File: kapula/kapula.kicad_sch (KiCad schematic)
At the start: 157 parts, among them J1 Conn_02x10_Odd_Even, J12 U.FL, J13 U.FL, J3 U.FL, J5 U.FL, J9 U.FL, Q1 AO3401A, Q1 BSS84, Q2 AO3401A, Q3 AO3400A, Q5 AO3400A, Q6 AO3400A, T1 BW21S7511A01TF, T2 BW21S7511A01TF, T3 BW21S7511A01TF, T4 BW21S7511A01TF, U1 XC6206P332MR, U2 TP4054, U3 DW01+G, U5 EFR32FG14P233F256GM48-B, U6 XA213-G4J, X1 DSB221SDN, Y1 32768 Hz

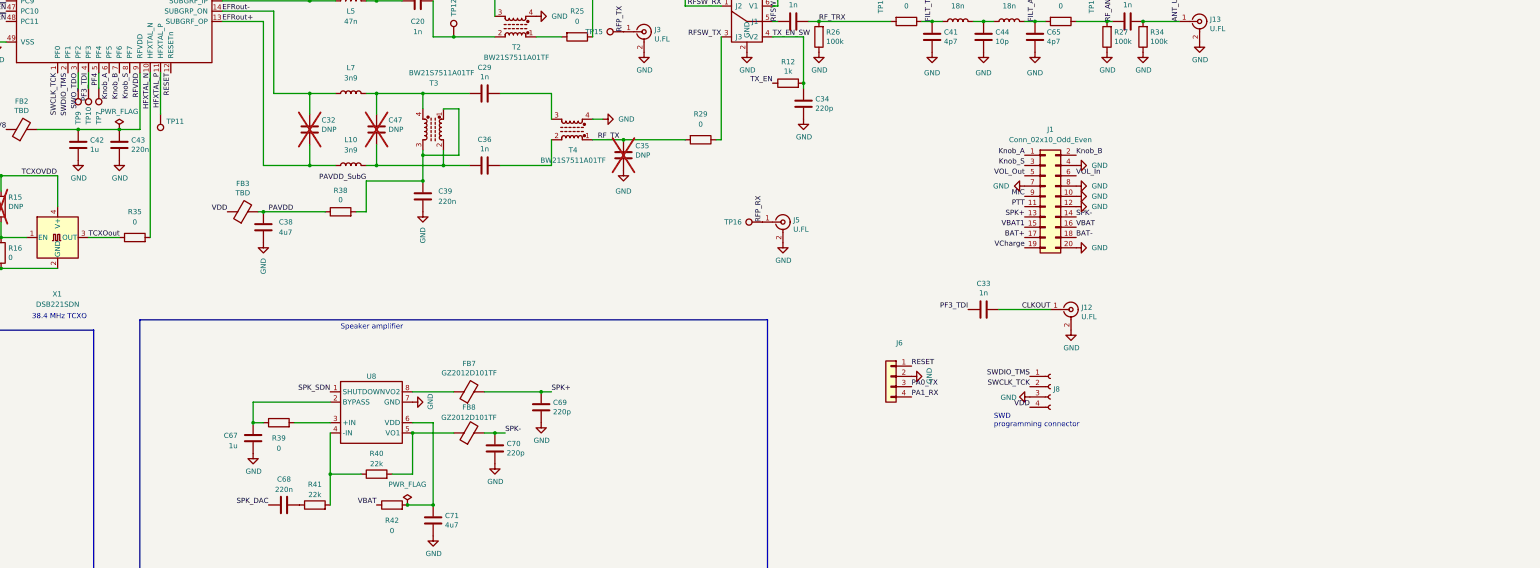
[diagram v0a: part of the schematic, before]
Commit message: Move components to make more space
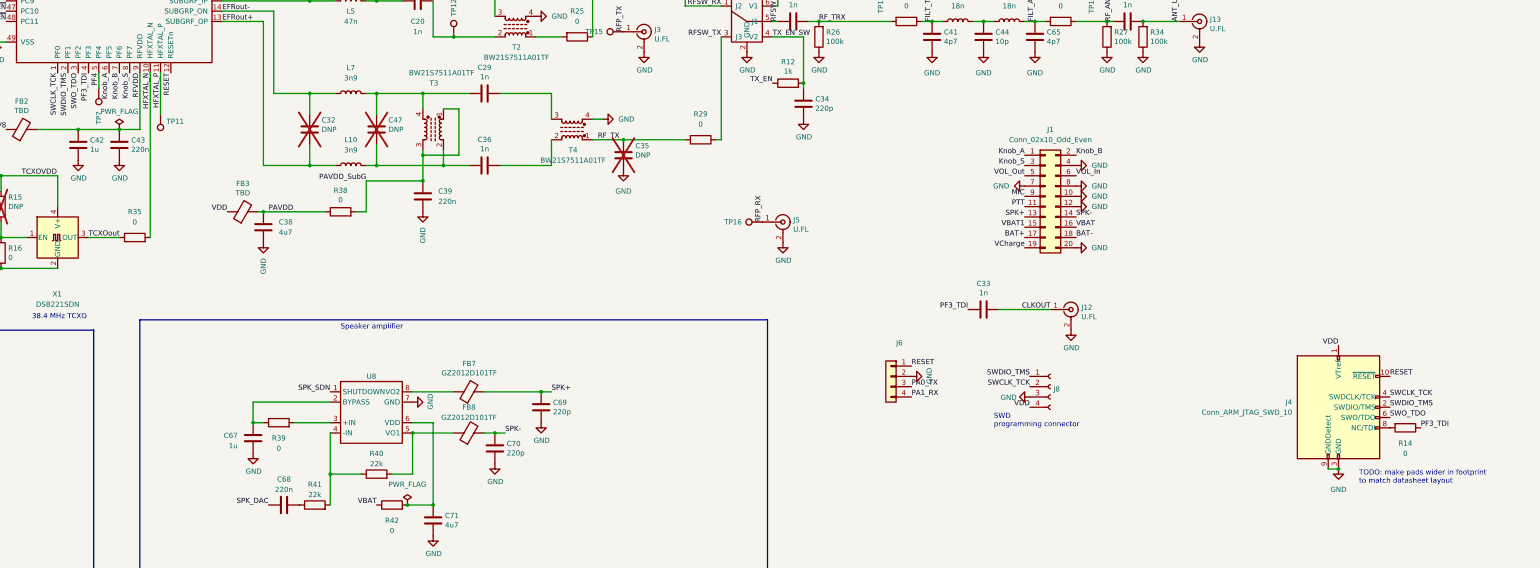
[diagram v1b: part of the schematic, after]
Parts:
- removed TP10, TP9: ~, TestPoint:TestPoint_Pad_D1.0mm, symbol Connector:TestPoint
- added J4: Conn_ARM_JTAG_SWD_10, Connector_PinHeader_1.27mm:PinHeader_2x05_P1.27mm_Vertical_SMD, symbol Connector:Conn_ARM_JTAG_SWD_10
- added R14: 0, kapula:R_0402_to_0603_HandSolder, symbol Device:R
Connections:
- net GND: now also J4.3 (GND), J4.5 (GND), J4.9 (GNDDetect)
- net PF3_TDI: now also R14.1
- net RESET: now also J4.10 (~{RESET})
- net SWCLK_TCK: now also J4.4 (SWDCLK/TCK)
- net SWDIO_TMS: now also J4.2 (SWDIO/TMS)
- net SWO_TDO: now also J4.6 (SWO/TDO)
- net VDD: now also J4.1 (VTref)
- new net: J4.8 (NC/TDI), R14.2
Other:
- note added: "TODO: make pads wider in footprint to match datasheet layout"
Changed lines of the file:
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@@
   (junction (at 201.93 127) (diameter 0) (color 0 0 0 0)
   )
+  (junction (at 439.42 252.73) (diameter 0) (color 0 0 0 0)
+  )
   (junction (at 173.99 82.55) (diameter 0) (color 0 0 0 0)
   )
@@
     (stroke (width 0) (type default))
   )
-  (wire (pts (xy 128.27 154.94) (xy 128.27 158.75))
-    (stroke (width 0) (type default))
-  )
   (wire (pts (xy 340.36 49.53) (xy 340.36 48.26))
     (stroke (width 0) (type default))
@@
     (stroke (width 0) (type default))
   )
+  (wire (pts (xy 436.88 252.73) (xy 439.42 252.73))
+    (stroke (width 0) (type default))
+  )
   (wire (pts (xy 353.06 30.48) (xy 365.76 30.48))
     (stroke (width 0) (type default))
@@
     (stroke (width 0) (type default))
   )
-  (wire (pts (xy 130.81 158.75) (xy 130.81 154.94))
-    (stroke (width 0) (type default))
-  )
   (wire (pts (xy 176.53 85.09) (xy 229.87 85.09))
     (stroke (width 0) (type default))
@@
     (effects (font (size 1.27 1.27)) (justify left bottom))
   )
+  (text "TODO: make pads wider in footprint\nto match datasheet layout"
+    (at 444.5 256.54 0)
+    (effects (font (size 1.27 1.27)) (justify left bottom))
+  )
   (text "38.4 MHz TCXO" (at 116.84 215.9 0)
     (effects (font (size 1.27 1.27)) (justify left bottom))
@@
     (effects (font (size 1.27 1.27)) (justify left bottom))
   )
+  (label "SWO_TDO" (at 452.12 240.03 0) (fields_autoplaced)
+    (effects (font (size 1.27 1.27)) (justify left bottom))
+  )
   (label "D_SCK" (at 110.49 134.62 180) (fields_autoplaced)
     (effects (font (size 1.27 1.27)) (justify right bottom))
@@
     (effects (font (size 1.27 1.27)) (justify left bottom))
   )
+  (label "RESET" (at 452.12 229.87 0) (fields_autoplaced)
+    (effects (font (size 1.27 1.27)) (justify left bottom))
+  )
   (label "PAVDD_2G4" (at 163.83 121.92 0) (fields_autoplaced)
     (effects (font (size 1.27 1.27)) (justify left bottom))
@@
     (effects (font (size 1.27 1.27)) (justify left bottom))
   )
+  (label "VDD" (at 439.42 222.25 180) (fields_autoplaced)
+    (effects (font (size 1.27 1.27)) (justify right bottom))
+  )
   (label "VBAT" (at 185.42 26.67 0) (fields_autoplaced)
     (effects (font (size 1.27 1.27)) (justify left bottom))
@@
     (effects (font (size 1.27 1.27)) (justify right bottom))
   )
+  (label "SWDIO_TMS" (at 452.12 237.49 0) (fields_autoplaced)
+    (effects (font (size 1.27 1.27)) (justify left bottom))
+  )
   (label "RFP_TX" (at 262.89 144.78 90) (fields_autoplaced)
     (effects (font (size 1.27 1.27)) (justify left bottom))
@@
     (effects (font (size 1.27 1.27)) (justify left bottom))
   )
+  (label "PF3_TDI" (at 459.74 242.57 0) (fields_autoplaced)
+    (effects (font (size 1.27 1.27)) (justify left bottom))
+  )
   (label "EFR_DECOUPLE" (at 110.49 124.46 180) (fields_autoplaced)
     (effects (font (size 1.27 1.27)) (justify right bottom))
@@
     (effects (font (size 1.27 1.27)) (justify right bottom))
   )
+  (label "SWCLK_TCK" (at 452.12 234.95 0) (fields_autoplaced)
+    (effects (font (size 1.27 1.27)) (justify left bottom))
+  )
   (label "Knob_A" (at 341.63 48.26 0) (fields_autoplaced)
     (effects (font (size 1.27 1.27)) (justify left bottom))
@@
     )
   )
-  (symbol (lib_id "Connector:TestPoint") (at 130.81 158.75 180) (unit 1)
-    (in_bom yes) (on_board yes) (dnp no)
-    (property "Reference" "TP10" (at 130.81 167.64 90)
-      (effects (font (size 1.27 1.27)) (justify right))
-    )
-    (property "Value" "~" (at 132.2832 161.7218 0)
-      (effects (font (size 1.27 1.27)) (justify right))
-    )
-    (property "Footprint" "TestPoint:TestPoint_Pad_D1.0mm" (at 125.73 158.75 0)
-      (effects (font (size 1.27 1.27)) hide)
-    )
-    (property "Datasheet" "" (at 125.73 158.75 0)
-      (effects (font (size 1.27 1.27)) hide)
-    )
-    (pin "1")
-    (instances
-      (project "kapula"
-        (path "/f2315993-072e-45c9-8c85-e79c6d40aba4"
-          (reference "TP10") (unit 1)
-        )
-      )
-    )
-  )
   (symbol (lib_id "power:GND") (at 78.74 34.29 0) (unit 1)
     (in_bom yes) (on_board yes) (dnp no)
@@
     )
   )
-  (symbol (lib_id "Connector:TestPoint") (at 128.27 158.75 180) (unit 1)
-    (in_bom yes) (on_board yes) (dnp no)
-    (property "Reference" "TP9" (at 128.27 167.64 90)
-      (effects (font (size 1.27 1.27)) (justify right))
-    )
-    (property "Value" "~" (at 129.7432 161.7218 0)
-      (effects (font (size 1.27 1.27)) (justify right))
-    )
-    (property "Footprint" "TestPoint:TestPoint_Pad_D1.0mm" (at 123.19 158.75 0)
-      (effects (font (size 1.27 1.27)) hide)
-    )
-    (property "Datasheet" "" (at 123.19 158.75 0)
-      (effects (font (size 1.27 1.27)) hide)
-    )
-    (pin "1")
-    (instances
-      (project "kapula"
-        (path "/f2315993-072e-45c9-8c85-e79c6d40aba4"
-          (reference "TP9") (unit 1)
-        )
-      )
-    )
-  )
   (symbol (lib_id "power:PWR_FLAG") (at 173.99 82.55 0) (unit 1)
     (in_bom yes) (on_board yes) (dnp no)
@@
     )
   )
+  (symbol (lib_id "Device:R") (at 455.93 242.57 270) (unit 1)
+    (in_bom yes) (on_board yes) (dnp no) (fields_autoplaced)
+    (property "Reference" "R14" (at 455.93 246.38 90)
+      (effects (font (size 1.27 1.27)))
+    )
+    (property "Value" "0" (at 455.93 248.92 90)
+      (effects (font (size 1.27 1.27)))
+    )
+    (property "Footprint" "kapula:R_0402_to_0603_HandSolder" (at 455.93 240.792 90)
+      (effects (font (size 1.27 1.27)) hide)
+    )
+    (property "Datasheet" "" (at 455.93 242.57 0)
+      (effects (font (size 1.27 1.27)) hide)
+    )
+    (property "LCSC" "C17168" (at 455.93 242.57 0)
+      (effects (font (size 1.27 1.27)) hide)
+    )
+    (pin "1")
+    (pin "2")
+    (instances
+      (project "kapula"
+        (path "/f2315993-072e-45c9-8c85-e79c6d40aba4"
+          (reference "R14") (unit 1)
+        )
+      )
+    )
+  )
   (symbol (lib_id "power:GND") (at 210.82 236.22 90) (unit 1)
     (in_bom yes) (on_board yes) (dnp no)
@@
     )
   )
+  (symbol (lib_id "Connector:Conn_ARM_JTAG_SWD_10") (at 439.42 237.49 0) (unit 1)
+    (in_bom yes) (on_board yes) (dnp no) (fields_autoplaced)
+    (property "Reference" "J4" (at 427.99 236.22 0)
+      (effects (font (size 1.27 1.27)) (justify right))
+    )
+    (property "Value" "Conn_ARM_JTAG_SWD_10" (at 427.99 238.76 0)
+      (effects (font (size 1.27 1.27)) (justify right))
+    )
+    (property "Footprint" "Connector_PinHeader_1.27mm:PinHeader_2x05_P1.27mm_Vertical_SMD" (at 439.42 237.49 0)
+      (effects (font (size 1.27 1.27)) hide)
+    )
+    (property "Datasheet" "https://datasheet.lcsc.com/lcsc/2209141730_DEALON-DZ127S-22-10-55_C5160761.pdf" (at 430.53 269.24 90)
+      (effects (font (size 1.27 1.27)) hide)
+    )
+    (property "LCSC" "C5160761" (at 439.42 237.49 0)
+      (effects (font (size 1.27 1.27)) hide)
+    )
+    (pin "1")
+    (pin "10")
+    (pin "2")
+    (pin "3")
+    (pin "4")
+    (pin "5")
+    (pin "6")
+    (pin "7")
+    (pin "8")
+    (pin "9")
+    (instances
+      (project "kapula"
+        (path "/f2315993-072e-45c9-8c85-e79c6d40aba4"
+          (reference "J4") (unit 1)
+        )
+      )
+    )
+  )
   (symbol (lib_id "Device:R") (at 251.46 124.46 270) (unit 1)
     (in_bom yes) (on_board yes) (dnp no) (fields_autoplaced)
@@
         )
       )
+    )
+  )
+  (symbol (lib_id "power:GND") (at 439.42 252.73 0) (unit 1)
+    (in_bom yes) (on_board yes) (dnp no) (fields_autoplaced)
+    (property "Reference" "#PWR042" (at 439.42 259.08 0)
+      (effects (font (size 1.27 1.27)) hide)
+    )
+    (property "Value" "GND" (at 439.42 257.81 0)
+      (effects (font (size 1.27 1.27)))
+    )
+    (property "Footprint" "" (at 439.42 252.73 0)
+      (effects (font (size 1.27 1.27)) hide)
+    )
+    (property "Datasheet" "" (at 439.42 252.73 0)
+      (effects (font (size 1.27 1.27)) hide)
+    )
+    (pin "1")
+    (instances
+      (project "kapula"
+        (path "/f2315993-072e-45c9-8c85-e79c6d40aba4"
+          (reference "#PWR042") (unit 1)
+        )
+      )
